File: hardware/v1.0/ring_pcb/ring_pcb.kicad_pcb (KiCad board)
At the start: 2 copper layers, 17.8 x 17.8 mm, 7 parts

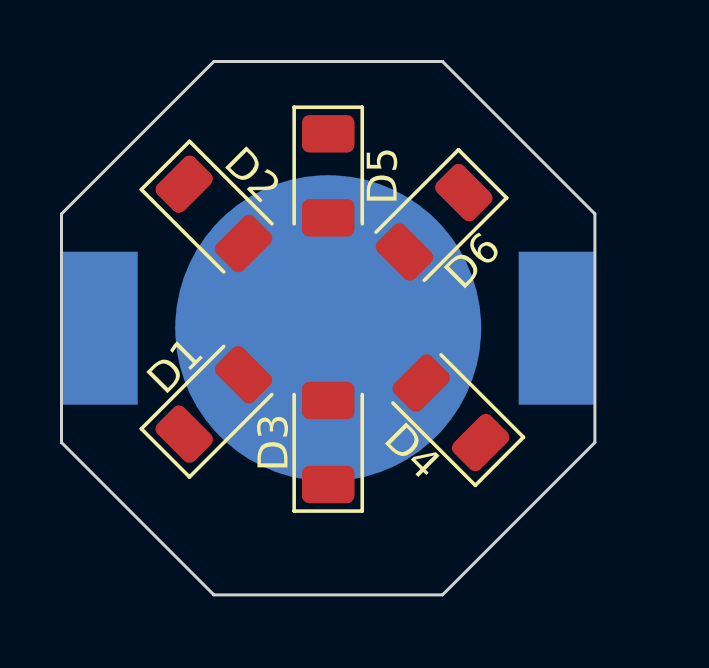
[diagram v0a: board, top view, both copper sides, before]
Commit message: Add test pads
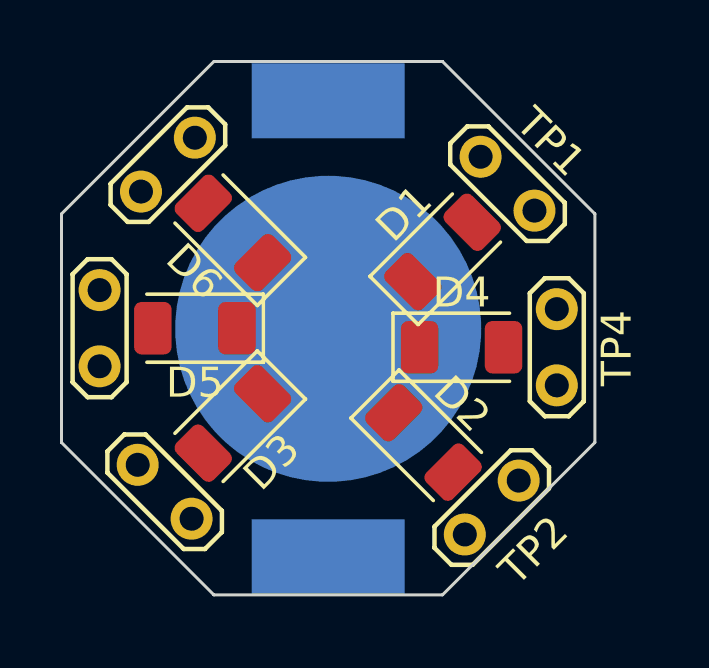
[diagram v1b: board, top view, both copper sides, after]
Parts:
- added TP1: TestPoint_2Pole, TestPoint:TestPoint_2Pads_Pitch2.54mm_Drill0.8mm, F.Cu at (142.2, 93.3)
- added TP2: TestPoint_2Pole, TestPoint:TestPoint_2Pads_Pitch2.54mm_Drill0.8mm, F.Cu at (143.5, 104.1)
- added TP3: TestPoint_2Pole, TestPoint:TestPoint_2Pads_Pitch2.54mm_Drill0.8mm, F.Cu at (132.6, 105.4)
- added TP4: TestPoint_2Pole, TestPoint:TestPoint_2Pads_Pitch2.54mm_Drill0.8mm, F.Cu at (144.8, 98.4)
- added TP5: TestPoint_2Pole, TestPoint:TestPoint_2Pads_Pitch2.54mm_Drill0.8mm, F.Cu at (129.5, 100.3)
- added TP6: TestPoint_2Pole, TestPoint:TestPoint_2Pads_Pitch2.54mm_Drill0.8mm, F.Cu at (132.7, 92.7)
- moved D2 10.3 mm to (140.3, 102.9)
- moved D1 9.16 mm to (141.0, 96.5)
- moved D5 6.75 mm to (132.7, 99.1), turned to 180 degrees
- moved D6 6.71 mm to (134.0, 95.9), turned to 135 degrees
- moved D3 3.24 mm to (134.0, 102.2), turned to -135 degrees
- moved D4 2.21 mm to (141.6, 99.7), turned to 0 degrees
- turned BT1 to -90 degrees

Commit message: First v0.1 cut
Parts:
- removed BT1: Battery_Cell, Battery:BatteryHolder_LINX_BAT-HLD-012-SMT
- added TP7: TestPoint_2Pole, Connector_Wire:SolderWirePad_1x02_P3.81mm_Drill1.2mm, F.Cu at (135.3, 92.1)
- added TP8: TestPoint_2Pole, Connector_Wire:SolderWirePad_1x02_P3.81mm_Drill1.2mm, F.Cu at (139.1, 106.0)
- moved TP6 3.59 mm to (130.2, 95.2), turned to 45 degrees
- moved TP2 1.42 mm to (144.1, 102.9)
- moved D1 1.42 mm to (139.7, 95.9)
- moved D2 0.90 mm to (139.7, 102.2)
- moved TP3 0.82 mm to (132.1, 104.8)
- moved D3 0.63 mm to (134.6, 102.2)
- moved D4 0.63 mm to (141.6, 99.1)
- moved D6 0.63 mm to (134.6, 95.9)
- moved TP4 0.63 mm to (144.8, 97.8)
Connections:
- net Net-(TP1-Pad1) renamed no_connect_8
- net Net-(TP2-Pad1) renamed no_connect_9
- net Net-(TP3-Pad1) renamed no_connect_10
- net Net-(TP4-Pad1) renamed no_connect_11
- net Net-(TP5-Pad1) renamed no_connect_12
- net Net-(TP6-Pad1) renamed no_connect_13
- D1 pad 1: Net-(D1-Pad1) -> GND
- D2 pad 1: Net-(D2-Pad1) -> GND
- D3 pad 1: Net-(D3-Pad1) -> GND
- D4 pad 1: Net-(D4-Pad1) -> GND
- D5 pad 1: Net-(D5-Pad1) -> GND
- D6 pad 1: Net-(D6-Pad1) -> GND
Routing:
- net GND: track 0.00 -> 27.3 mm
- net Net-(D3-Pad2): track 0.00 -> 3.45 mm
- net Net-(D1-Pad2): track 0.00 -> 3.45 mm
- net Net-(D5-Pad2): track 0.00 -> 2.30 mm
- net Net-(D4-Pad2): track 0.00 -> 2.30 mm
- net Net-(D6-Pad2): track 0.00 -> 2.26 mm
- net Net-(D2-Pad2): track 0.00 -> 2.26 mm
- added copper zone on F.Cu, net GND
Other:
- board text added: "Lantern Ring v0.1 OSHW TAPR designed by whatnick"
